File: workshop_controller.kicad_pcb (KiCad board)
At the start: 4 copper layers, 184.9 x 88 mm, 60 parts, among them J1 Conn_02x10_Odd_Even, J2 Conn_02x10_Odd_Even, J3 AudioJack3, J4 Micro_SD_Card, J5 Conn_02x25_Odd_Even, J6 Conn_01x05_Female, J7 LOGO_TOUCH, M1 Microphone4, SW1 SW_Push, SW2 SW_Push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

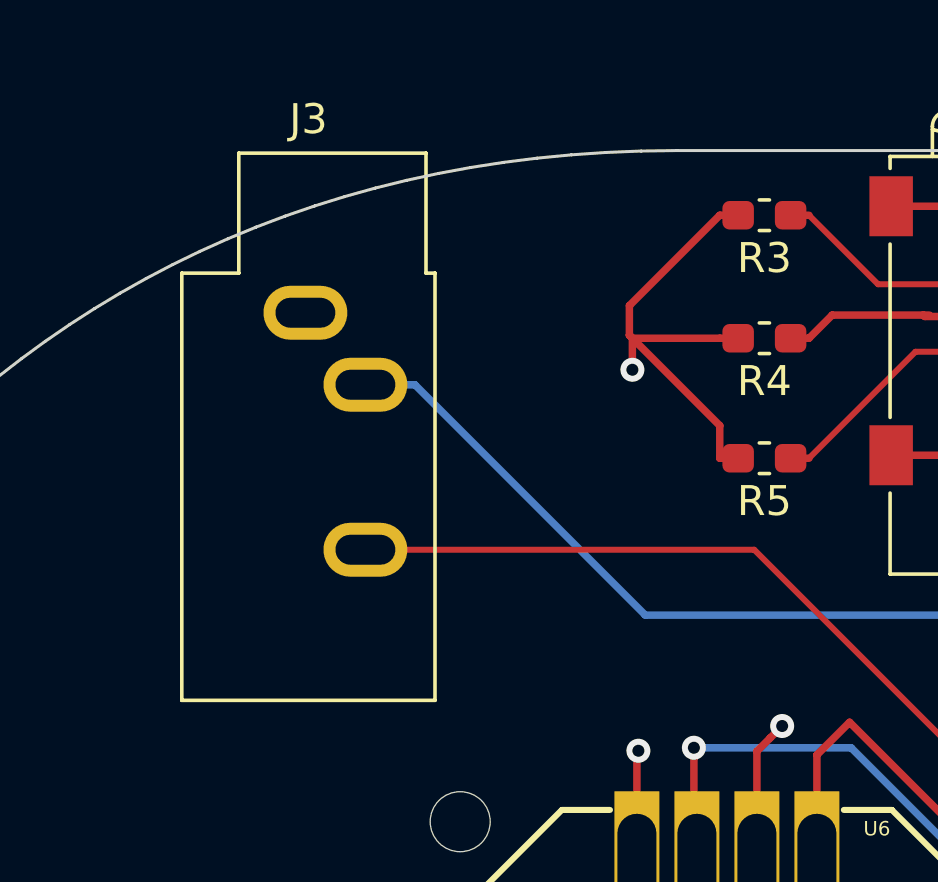
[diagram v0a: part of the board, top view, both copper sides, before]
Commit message: Add pin numbers to esp32
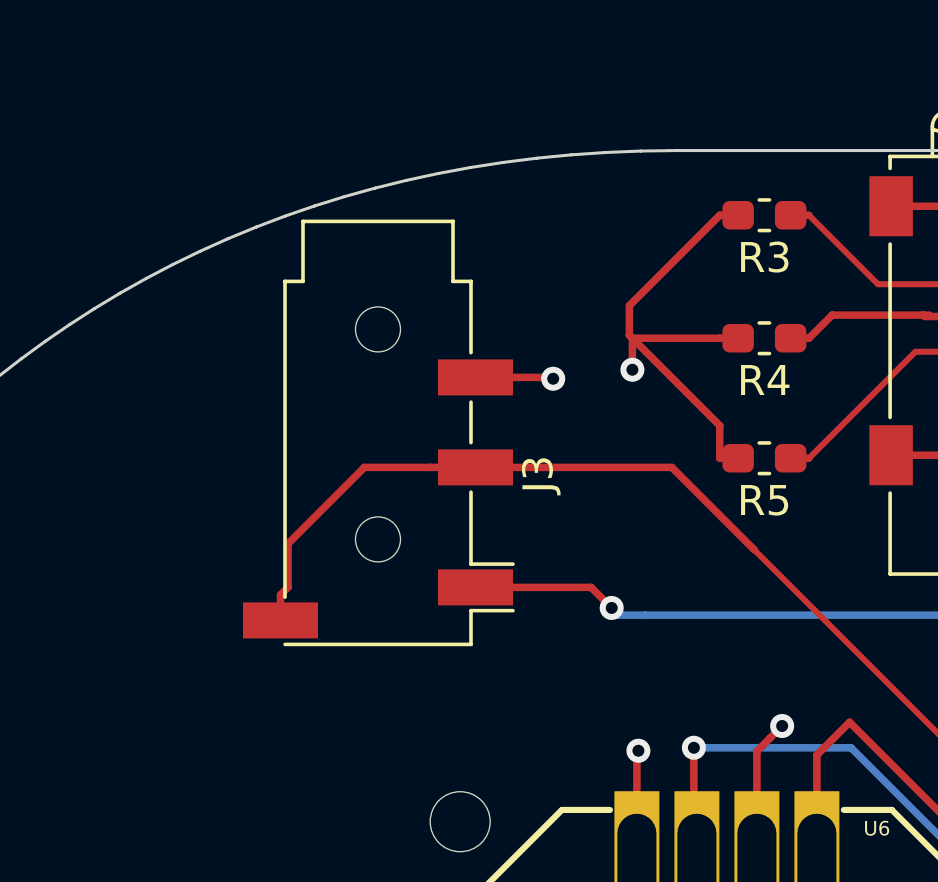
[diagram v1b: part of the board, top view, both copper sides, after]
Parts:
- J3: value AudioJack3 -> AudioJack4; footprint Connector_Audio:Jack_3.5mm_CUI_SJ1-3533NG_Horizontal -> Connector_Audio:Jack_3.5mm_PJ320D_Horizontal
- moved J3 5.85 mm to (90.4, 63.8), turned to 270 degrees
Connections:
- net /PIN_TMS renamed /PIN_TMS_14
- net /PIN_VN renamed /PIN_VN_39
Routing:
- net /PIN_26: track 95.8 -> 103.2 mm
- net /PIN_25: track 60.8 -> 54.3 mm, vias 1 -> 2
- net GND: track 139.0 -> 141.6 mm, vias 25 -> 26

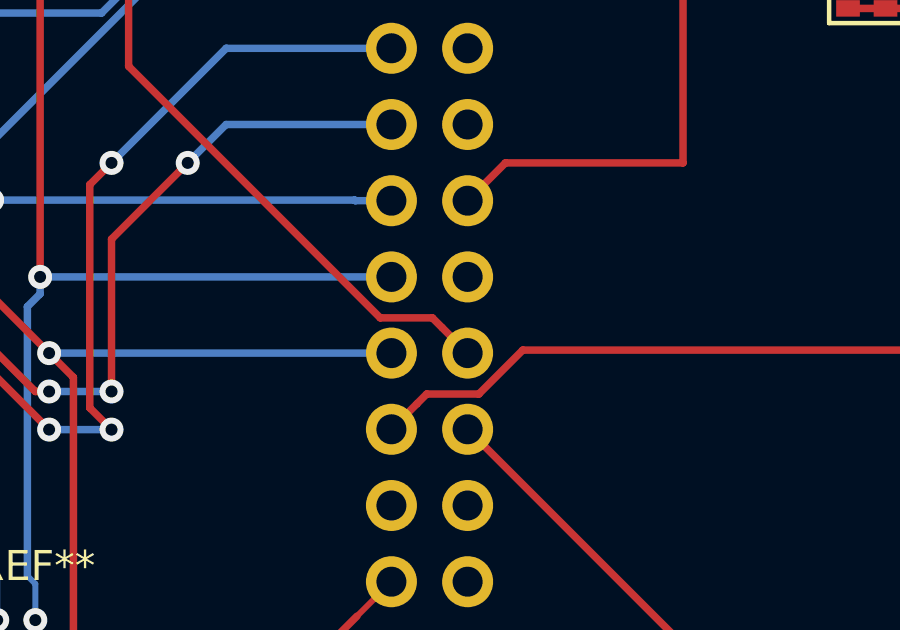
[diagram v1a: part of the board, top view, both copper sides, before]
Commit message: Change SPI header CS to 33
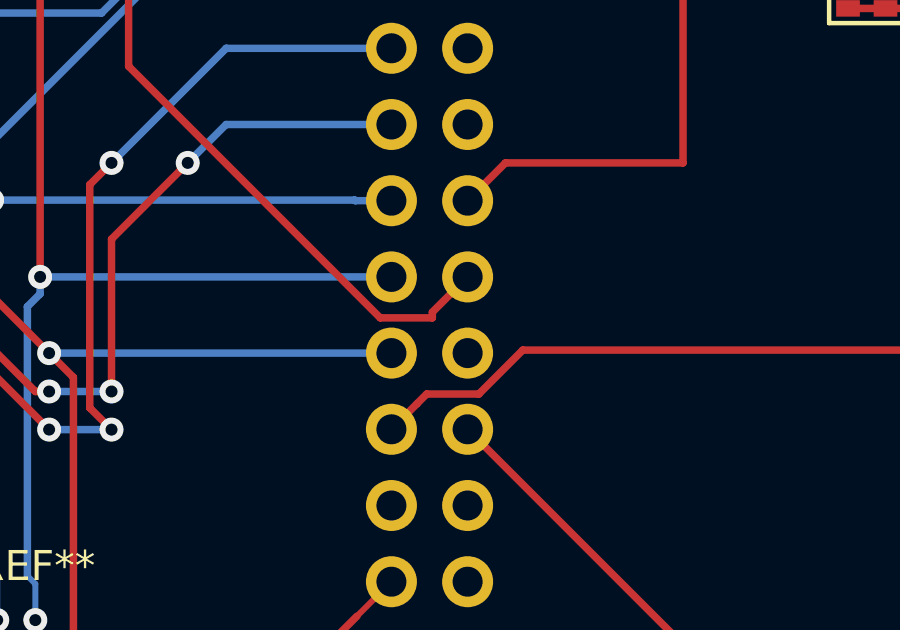
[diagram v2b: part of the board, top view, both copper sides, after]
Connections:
- J1 pad 11: /PIN_34 -> /INPUT_ONLY
- SPI_HEADER1 pad 2: /PIN_34 -> /PIN_33
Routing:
- net /PIN_33: track 0.00 -> 52.1 mm, vias 0 -> 2
- net /PIN_34: track 51.9 -> 0.00 mm, vias 2 -> 0

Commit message: Change a bunch of pins
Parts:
- removed G***: LOGO, Hackheim_logo:F.Silk_g9874
- removed G***: LOGO, Hackheim_logo:F.Mask_g9872
- removed G***: LOGO, Hackheim_logo:ndc_logo_oslo
- removed svg2mod: G***, svg2mod
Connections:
- net /PIN_RXD renamed /PIN_RXD_03
- net /PIN_TXD renamed /PIN_TXD_01
- J1 pad 11: /INPUT_ONLY -> /JOY_Y
- J1 pad 15: Net-(J1-Pad15) -> /NC
- J1 pad 19: /JOY_Y -> /PIN_CMD_11
- J1 pad 20: /LED_DA -> /PIN_SD3_10
- J1 pad 3: Net-(J1-Pad3) -> /NC
- J1 pad 4: /PIN_AMP_SHUTDOWN -> /PIN_VP_36
- J1 pad 5: /PIN_VN_39 -> /JOY_X
- J2 pad 12: /PIN_4 -> /LED_DA
- J2 pad 20: /JOY_X -> /PIN_CLK_06
- J4 pad 2: /PIN_2 -> /PIN_TMS_14
- J5 pad 13: /PIN_4 -> /PIN_0
- J5 pad 15: /PIN_SD1_08 -> /PIN_TDO_15
- J5 pad 41: /PIN_SDO_07 -> /PIN_5
- R4 pad 1: /PIN_2 -> /PIN_TMS_14
- SW1 pad 2: /PIN_5 -> /PIN_VP_36
- SW2 pad 2: /PIN_TMS_14 -> /SW2_PIN
- SW5 pad 2: /PIN_5 -> /PIN_VP_36
- SW6 pad 2: /PIN_TMS_14 -> /SW2_PIN
- U3 pad 21: /SW3_PIN -> /SW2_PIN
- U3 pad 22: /SW4_PIN -> /SW3_PIN
- U3 pad 23: Net-(U3-Pad23) -> /SW4_PIN
- U4 pad 1: /PIN_AMP_SHUTDOWN -> /PIN_2
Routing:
- net /PIN_5: track 44.4 -> 11.2 mm
- net /PIN_TMS_14: track 46.8 -> 29.6 mm
- net /JOY_Y: track 86.0 -> 93.1 mm
- net /SW4_PIN: track 80.4 -> 73.8 mm
- net /PIN_AMP_SHUTDOWN: track 58.7 -> 52.6 mm
- net /PIN_2: track 56.4 -> 52.5 mm
- net /PIN_4: track 29.8 -> 27.0 mm
- net /JOY_X: track 53.6 -> 52.4 mm
- net /LED_DA: track 37.4 -> 36.2 mm
- net /PIN_SD1_08: track 30.2 -> 29.3 mm
- net /PIN_SDO_07: track 25.4 -> 24.5 mm
- net /SW3_PIN: track 52.9 -> 52.3 mm

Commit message: Move I2C pullup pins closer to esp32
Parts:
- moved R2 86.2 mm to (140.2, 76.2)
- moved R1 85.0 mm to (140.2, 81.2)
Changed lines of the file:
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@@
   )
   (module Resistor_SMD:R_0603_1608Metric_Pad1.05x0.95mm_HandSolder (layer F.Cu)
-    (at 223.57 64.85 270)
+    (at 140.17 81.25 270)
     (descr "Resistor SMD 0603 (1608 Metric), square (rectangular) end terminal, IPC_7351 nominal with elongated pad for handsoldering. (Body size source: http://www.tortai-tech.com/upload/download/2011102023233369053.pdf), generated with kicad-footprint-generator")
     (tags "resistor handsolder")
@@
   )
   (module Resistor_SMD:R_0603_1608Metric_Pad1.05x0.95mm_HandSolder (layer F.Cu)
-    (at 225.985 67.66 180)
+    (at 140.23 76.23 180)
     (descr "Resistor SMD 0603 (1608 Metric), square (rectangular) end terminal, IPC_7351 nominal with elongated pad for handsoldering. (Body size source: http://www.tortai-tech.com/upload/download/2011102023233369053.pdf), generated with kicad-footprint-generator")
     (tags "resistor handsolder")

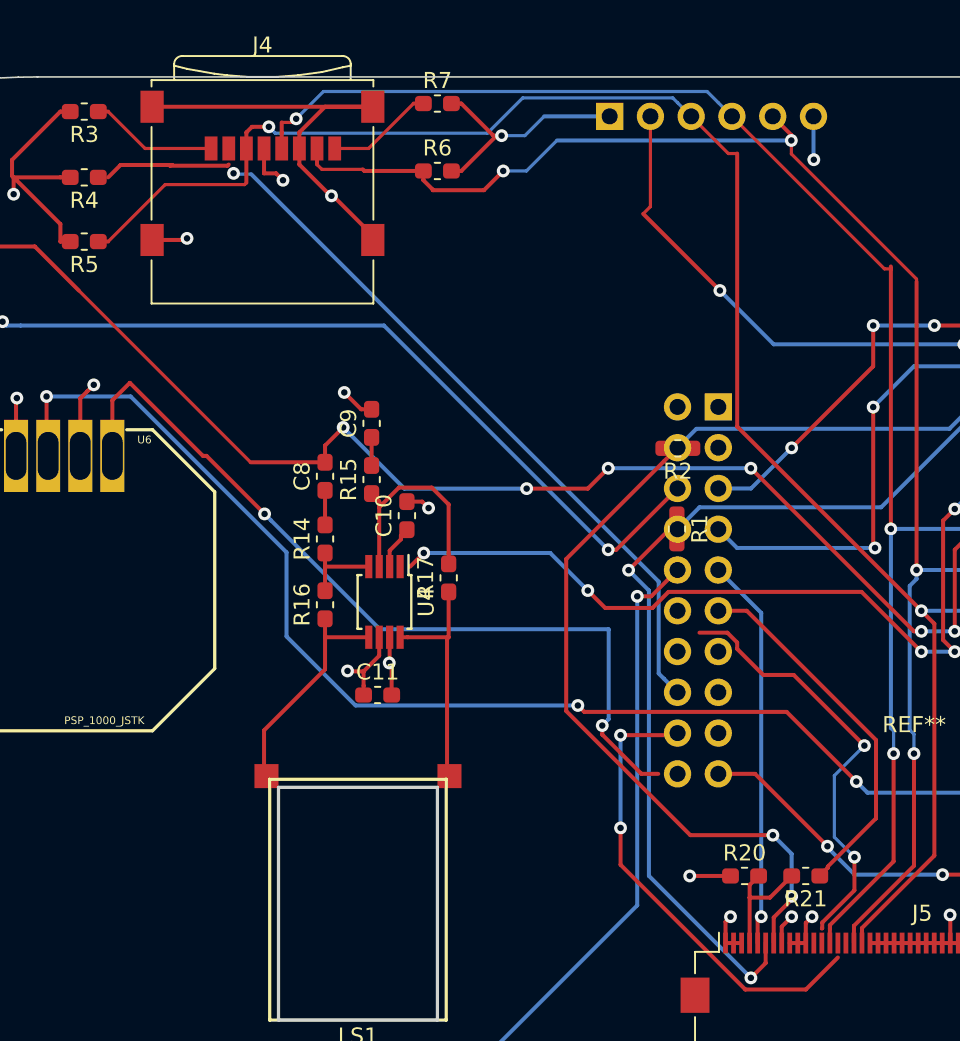
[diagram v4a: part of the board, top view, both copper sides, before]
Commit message: Swap SPI_SDI and SPI_SDO
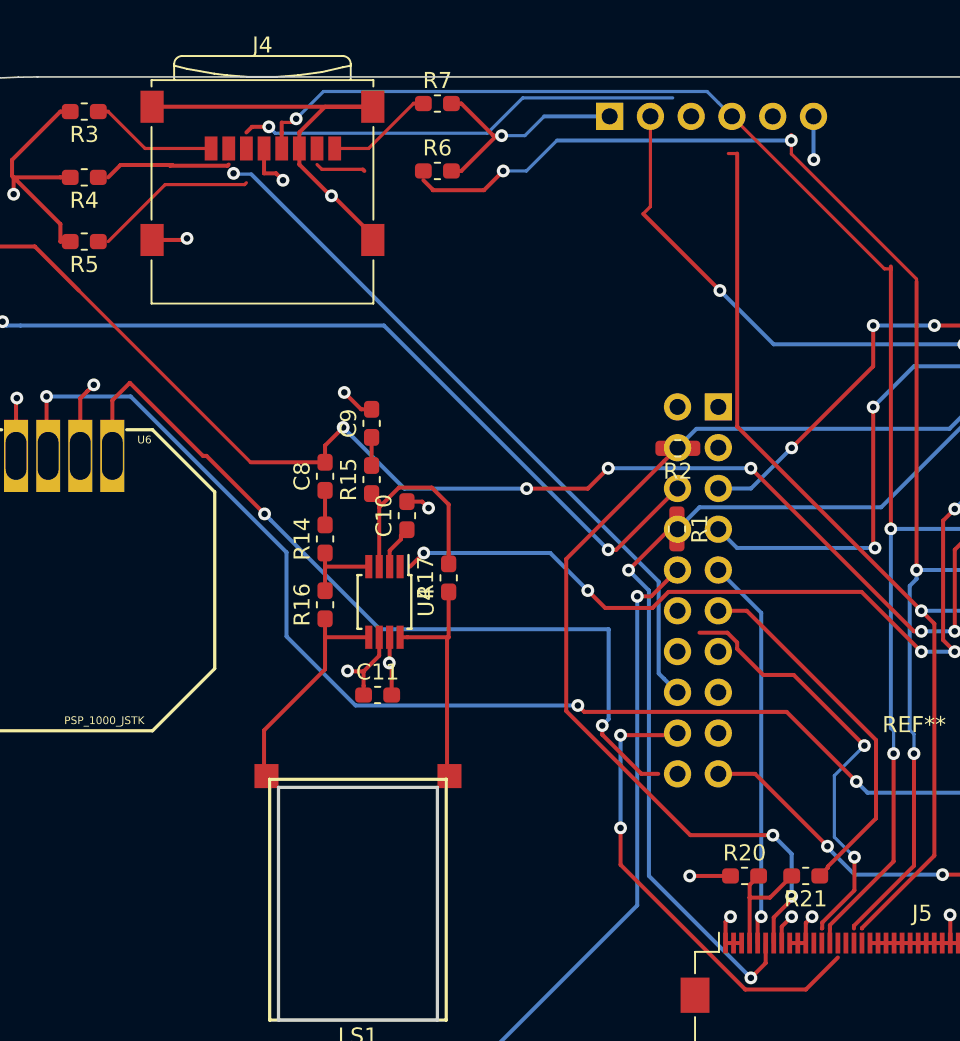
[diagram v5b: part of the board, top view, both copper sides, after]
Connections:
- J4 pad 3: /PIN_23 -> /PIN_19
- J4 pad 7: /PIN_19 -> /PIN_23
- J5 pad 17: /PIN_19 -> /PIN_23
- J5 pad 18: /PIN_23 -> /PIN_19
- R5 pad 1: /PIN_23 -> /PIN_19
- R6 pad 1: /PIN_19 -> /PIN_23
- SPI_HEADER1 pad 3: /PIN_23 -> /PIN_19
- SPI_HEADER1 pad 5: /PIN_19 -> /PIN_23
- SW1 pad 2: /PIN_VP_36 -> /SW1_PIN
- SW5 pad 2: /PIN_VP_36 -> /SW1_PIN
- U3 pad 21: /SW2_PIN -> /SW1_PIN
- U3 pad 22: /SW3_PIN -> /SW2_PIN
- U3 pad 23: /SW4_PIN -> /SW3_PIN
- U3 pad 24: Net-(U3-Pad24) -> /SW4_PIN
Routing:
- net /PIN_23: track 114.7 -> 105.1 mm
- net /PIN_19: track 101.6 -> 93.8 mm

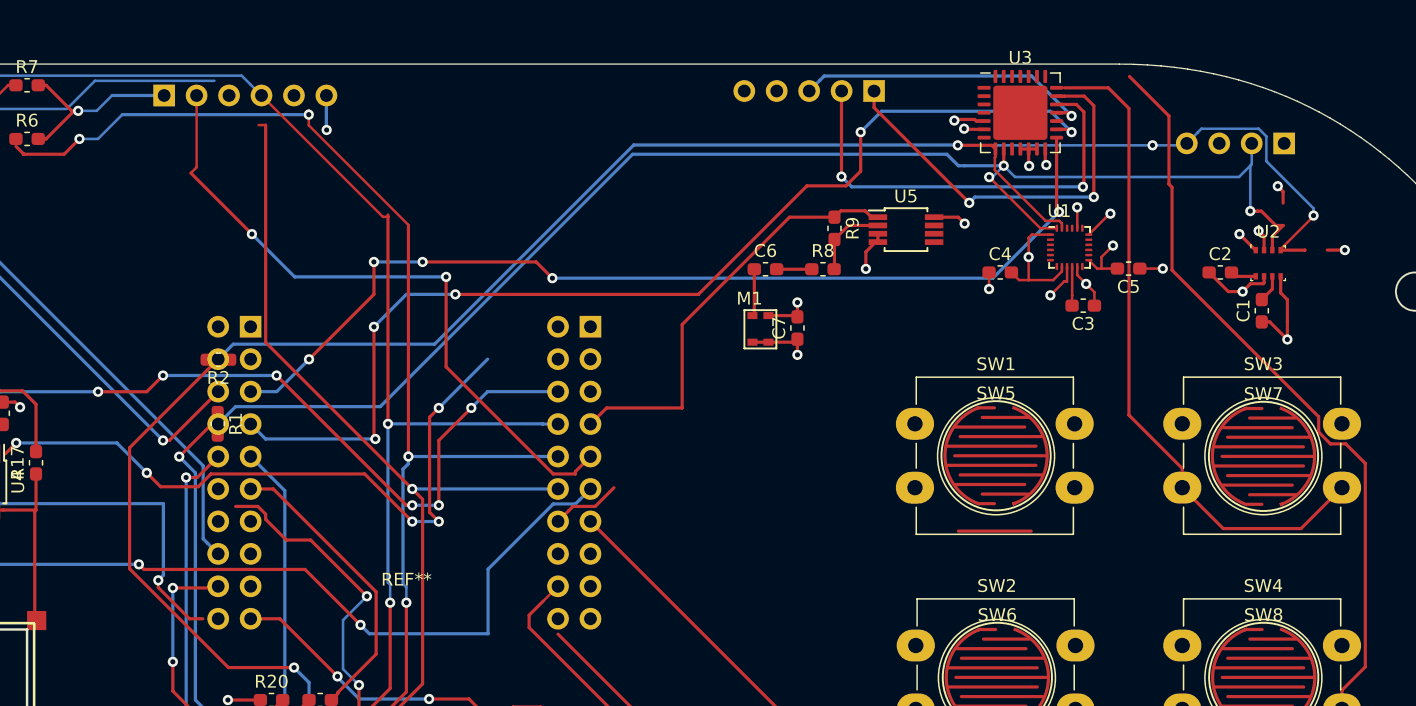
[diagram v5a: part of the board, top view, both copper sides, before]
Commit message: Use smd headers
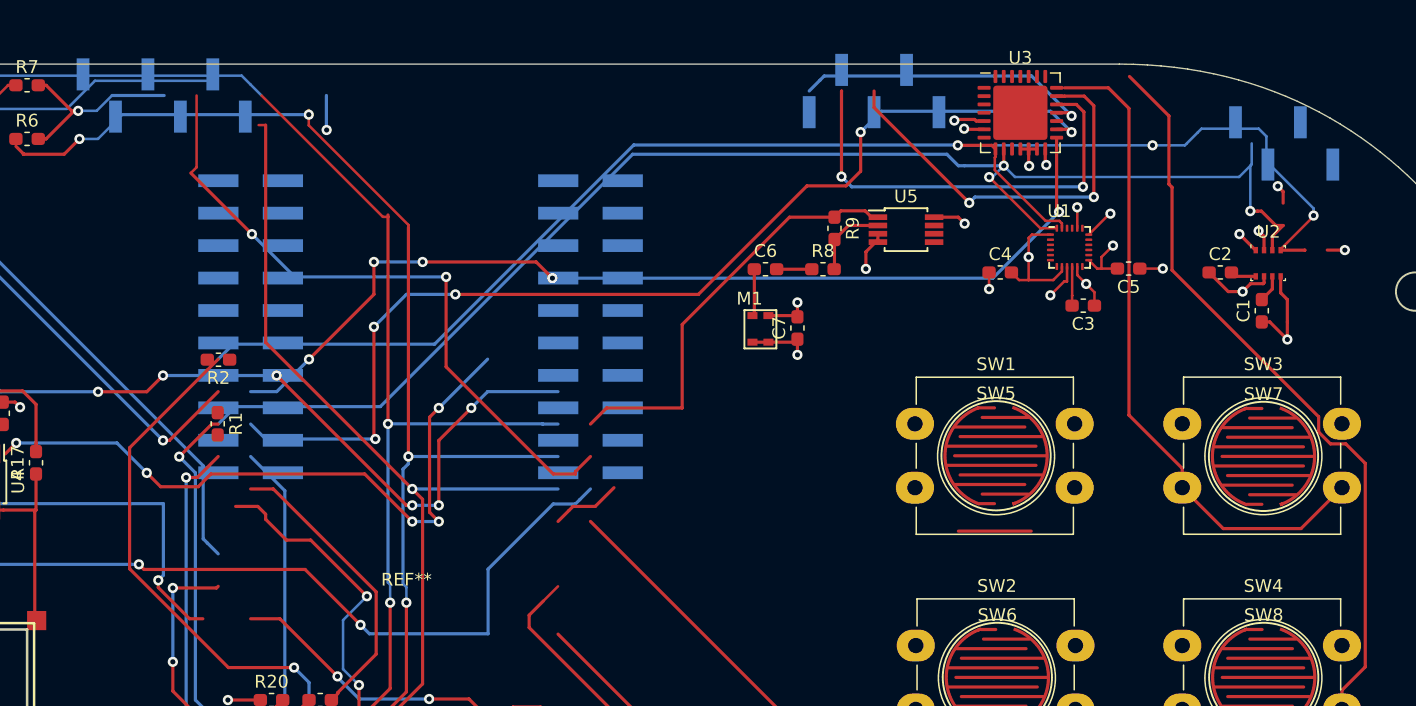
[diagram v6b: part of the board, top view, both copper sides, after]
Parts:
- I2C_HEADER1: footprint Connector_PinHeader_2.54mm:PinHeader_1x04_P2.54mm_Horizontal -> Connector_PinHeader_2.54mm:PinHeader_1x04_P2.54mm_Vertical_SMD_Pin1Left
- J1, J2: footprint Connector_PinHeader_2.54mm:PinHeader_2x10_P2.54mm_Vertical -> Connector_PinHeader_2.54mm:PinHeader_2x10_P2.54mm_Vertical_SMD
- J6: footprint Connector_PinHeader_2.54mm:PinHeader_1x05_P2.54mm_Horizontal -> Connector_PinHeader_2.54mm:PinHeader_1x05_P2.54mm_Vertical_SMD_Pin1Left
- SPI_HEADER1: footprint Connector_PinSocket_2.54mm:PinSocket_1x06_P2.54mm_Vertical -> Connector_PinHeader_2.54mm:PinHeader_1x06_P2.54mm_Vertical_SMD_Pin1Left
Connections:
- J4 pad 3: /PIN_19 -> /SPI_SDO
- J4 pad 7: /PIN_23 -> /SPI_SDI
- R5 pad 1: /PIN_19 -> /SPI_SDO
- R6 pad 1: /PIN_23 -> /SPI_SDI
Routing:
- net /GE_INTA: track 84.4 -> 136.5 mm, vias 5 -> 7
- net /PIN_33: track 52.1 -> 0.00 mm, vias 2 -> 0
